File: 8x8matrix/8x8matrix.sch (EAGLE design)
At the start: 21 parts

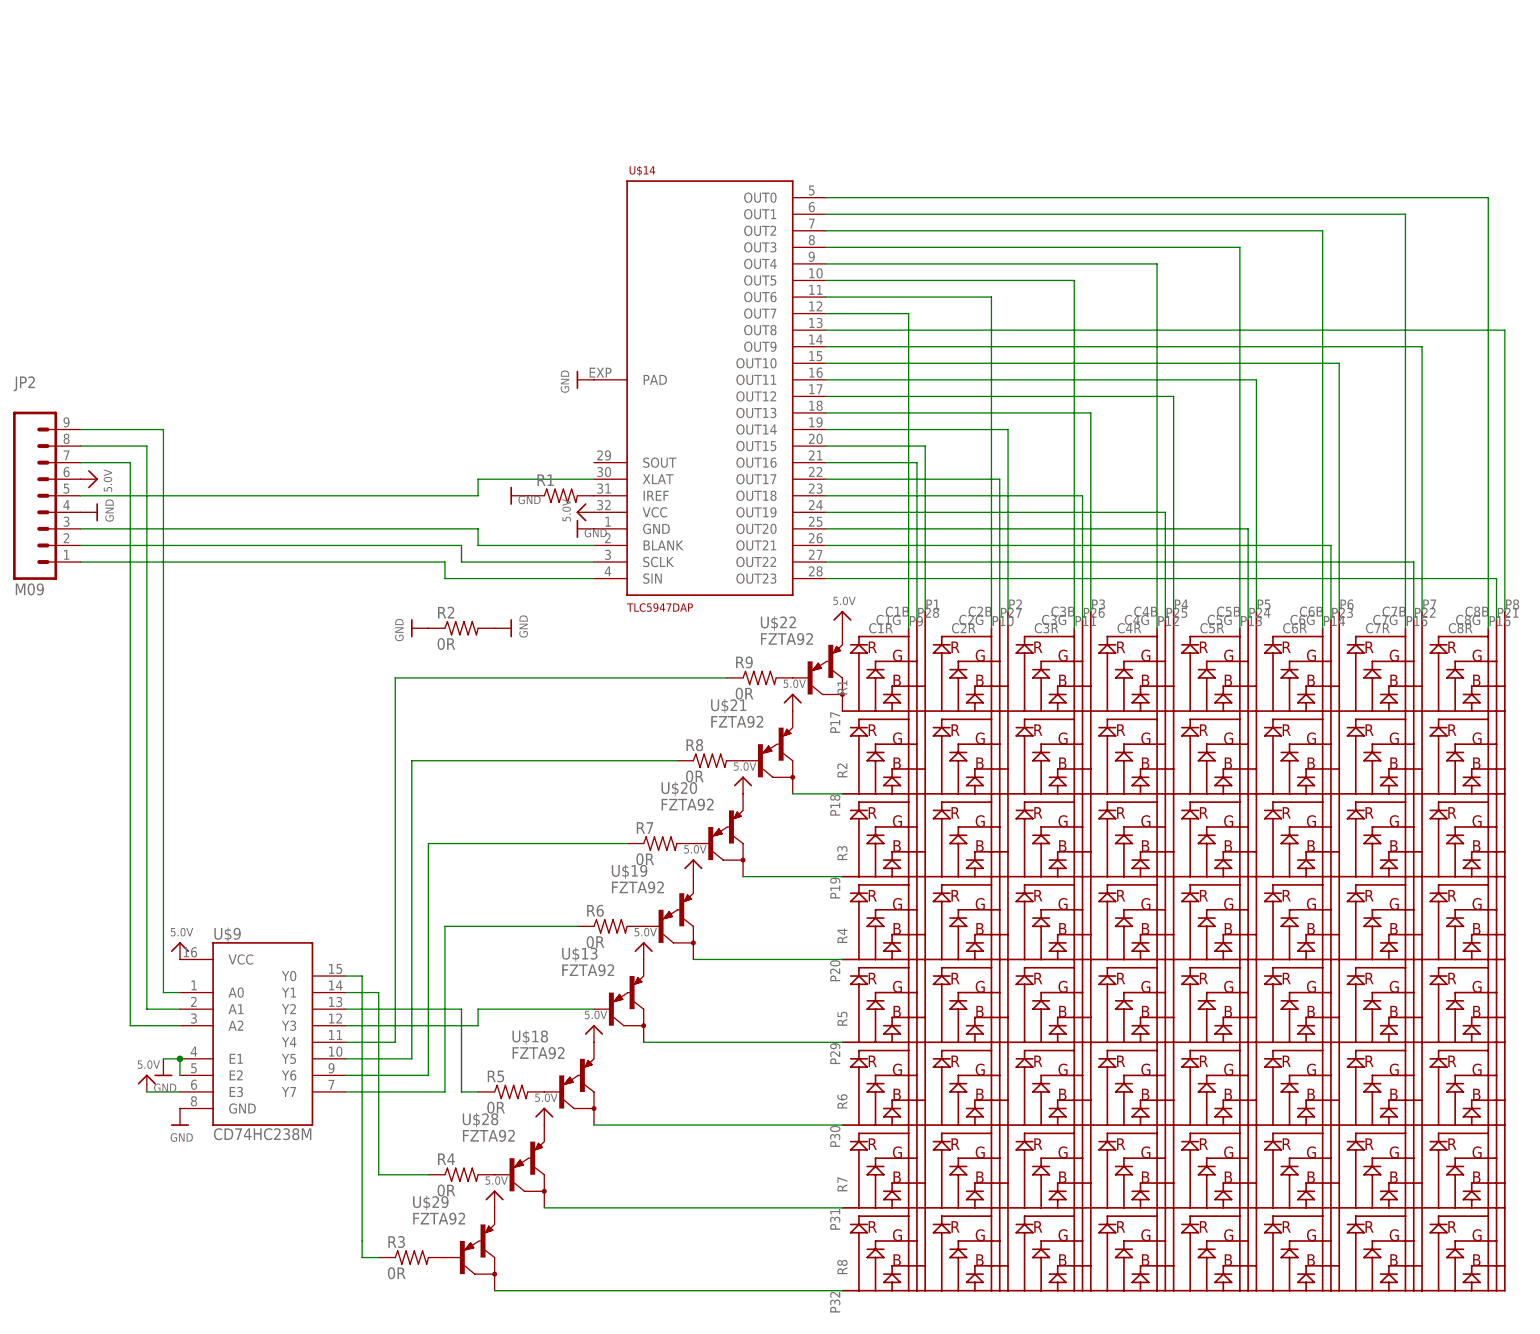
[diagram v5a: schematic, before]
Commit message: tried with regular SOT23 PNPs
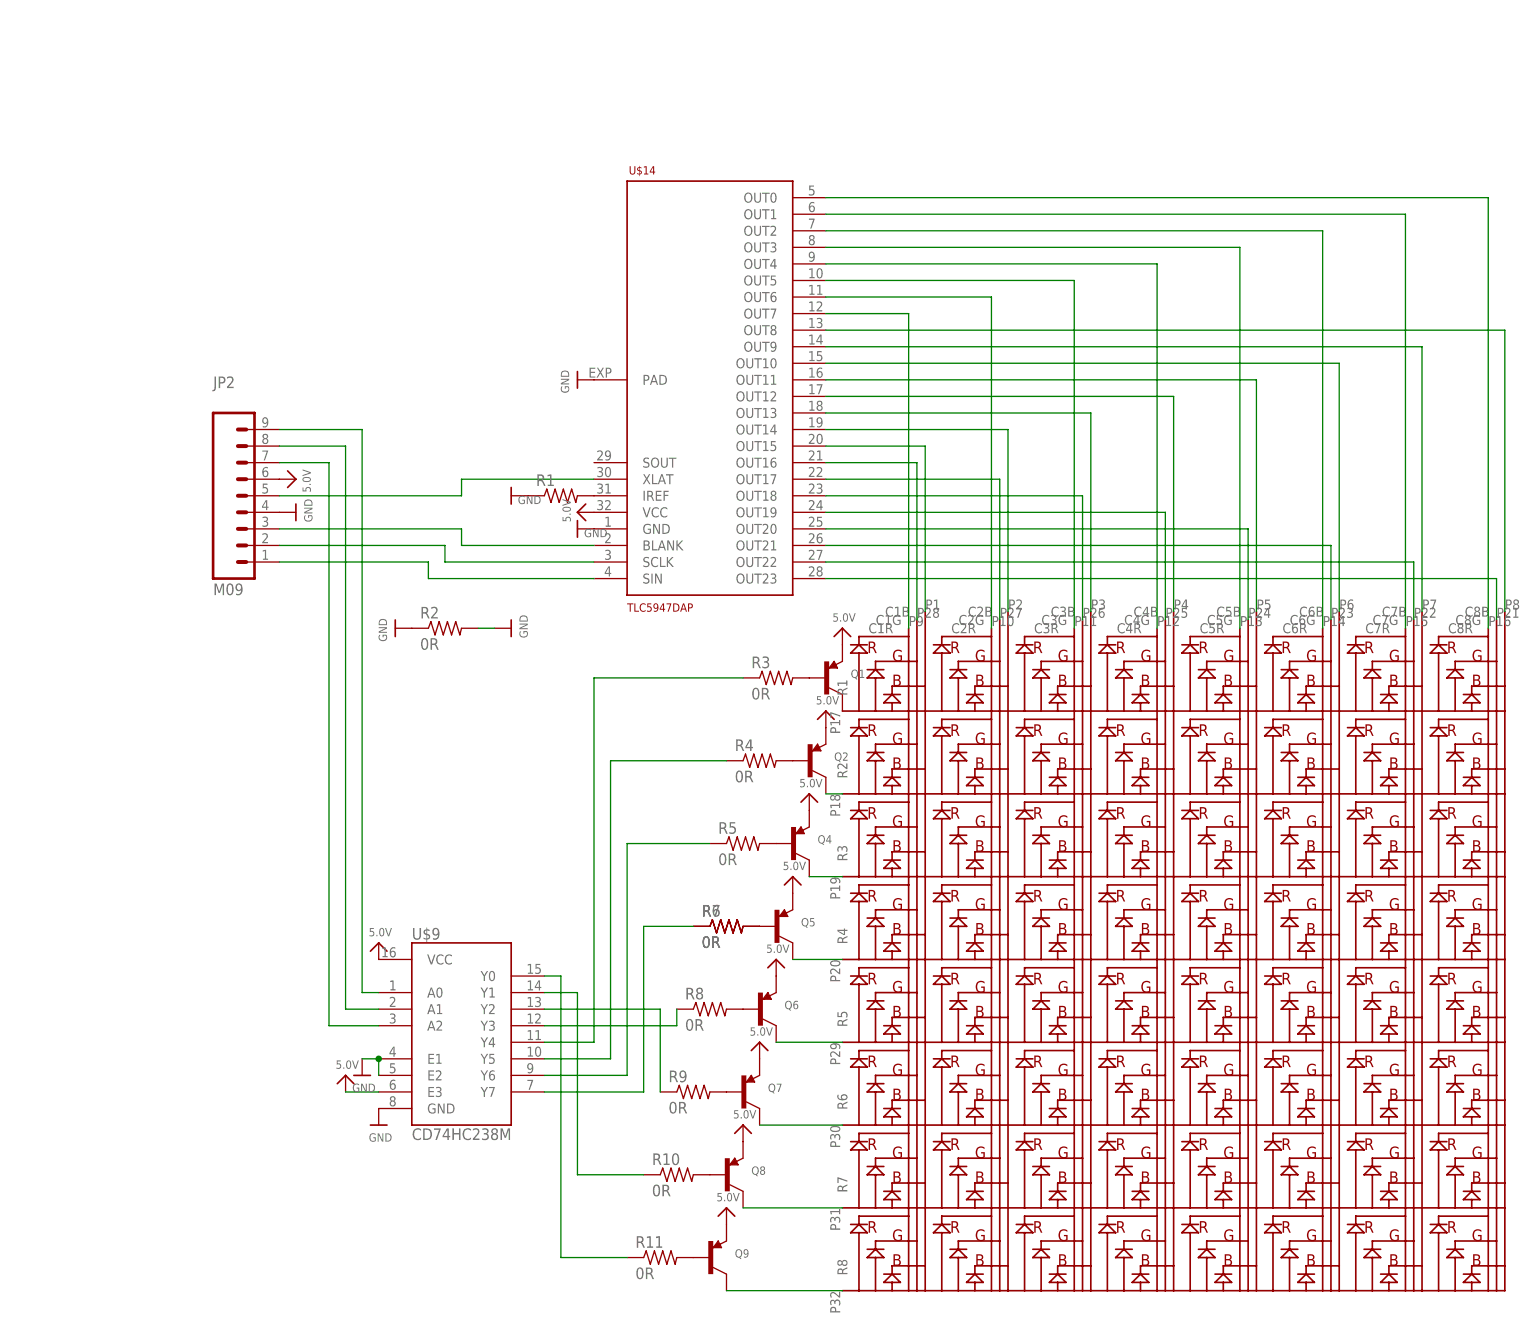
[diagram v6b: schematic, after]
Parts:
- removed U$13, U$18, U$19, U$20, U$21, U$22, U$28, U$29: FZTA92, mylib:FZTA92
- added Q1, Q2, Q4, Q5, Q6, Q7, Q8, Q9: (no value), microbuilder:TRANSISTOR_PNPSOT23-WAVE
- added R10, R11: 0R, resistor:R-US_M1206
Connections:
- new net N$52: Q9.C, U$1.R8
- net 5.0V: now also Q1.E, Q2.E, Q4.E, Q5.E, Q6.E, Q7.E, Q8.E, Q9.E; no longer U$13.E, U$18.E, U$19.E, U$20.E, U$21.E, U$22.E, U$28.E, U$29.E
- net N$25: no longer U$13.B
- net N$26: now also R7.1
- net N$28: now also Q1.C, U$1.R1; no longer R5.2, U$18.B
- net N$29: now also R5.1; no longer R7.1
- net N$30: now also R4.1; no longer R8.1
- net N$31: now also R3.1; no longer R9.1
- net N$32: now also Q4.B, R5.2; no longer U$1.R5, U$13.C
- net N$33: no longer R5.1
- net N$34: now also R10.1; no longer R4.1
- net N$35: now also R11.1; no longer R3.1
- net N$39: now also Q7.B, R9.2; no longer R7.2, U$20.B
- net N$40: now also Q8.B, R10.2; no longer R8.2, U$21.B
- net N$41: now also Q1.B, R3.2; no longer R9.2, U$22.B
- net N$42: now also Q2.B, R4.2; no longer U$1.R6, U$18.C
- net N$43: now also Q5.B, R6.2, R7.2; no longer U$1.R1, U$22.C
- net N$44: now also Q2.C; no longer U$21.C
- net N$45: now also Q6.B, R8.2; no longer R6.2, U$19.B
- net N$46: now also Q9.B, R11.2; no longer U$1.R3, U$20.C
- net N$47: now also Q5.C; no longer U$19.C
- net N$48: now also Q4.C, U$1.R3; no longer R4.2, U$28.B
- net N$49: now also Q6.C, U$1.R5; no longer R3.2, U$29.B
- net N$50: now also Q7.C, U$1.R6; no longer U$1.R7, U$28.C
- net N$51: now also Q8.C, U$1.R7; no longer U$1.R8, U$29.C
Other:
- moved on the sheet: JP2, R2, R3, R4, R5, R6, R7, R8, R9, U$9

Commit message: tried with BCR198S pnp arrays
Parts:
- removed Q1, Q2, Q4, Q5, Q6, Q7, Q8, Q9: (no value), microbuilder:TRANSISTOR_PNPSOT23-WAVE
- removed R10, R11, R3, R4, R5, R6, R7, R8, R9: 0R, resistor:R-US_M1206
- added U$13, U$17, U$18, U$19: BCR198S, mylib:BCR198S
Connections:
- removed net N$42: Q2.B, R4.2
- removed net N$43: Q5.B, R6.2, R7.2
- removed net N$44: Q2.C, U$1.R2
- removed net N$45: Q6.B, R8.2
- removed net N$46: Q9.B, R11.2
- removed net N$48: Q4.C, U$1.R3
- removed net N$49: Q6.C, U$1.R5
- removed net N$51: Q8.C, U$1.R7
- net 5.0V: now also R2.1, R2.2, U$13G$1.E, U$13G$2.E, U$17G$1.E, U$17G$2.E, U$18G$1.E, U$18G$2.E, U$19G$2.E; no longer Q1.E, Q2.E, Q4.E, Q5.E, Q6.E, Q7.E, Q8.E, Q9.E
- net GND: no longer R2.1, R2.2
- net N$25: now also U$18G$1.B
- net N$26: now also U$17G$2.B; no longer R6.1, R7.1
- net N$28: now also U$1.R3, U$17G$1.C; no longer Q1.C, U$1.R1
- net N$29: now also U$17G$1.B; no longer R5.1
- net N$30: now also U$13G$2.B; no longer R4.1
- net N$31: now also U$13G$1.B; no longer R3.1
- net N$32: now also U$1.R2, U$13G$2.C; no longer Q4.B, R5.2
- net N$33: now also U$18G$2.B
- net N$34: now also U$19G$1.B; no longer R10.1
- net N$35: now also U$19G$2.B; no longer R11.1
- net N$39: now also U$1.R1, U$13G$1.C; no longer Q7.B, R9.2
- net N$40: now also U$1.R5, U$18G$1.C; no longer Q8.B, R10.2
- net N$41: now also U$1.R7, U$19G$1.C; no longer Q1.B, R3.2
- net N$47: now also U$17G$2.C; no longer Q5.C
- net N$50: now also U$18G$2.C; no longer Q7.C
- net N$52: now also U$19G$2.C; no longer Q9.C

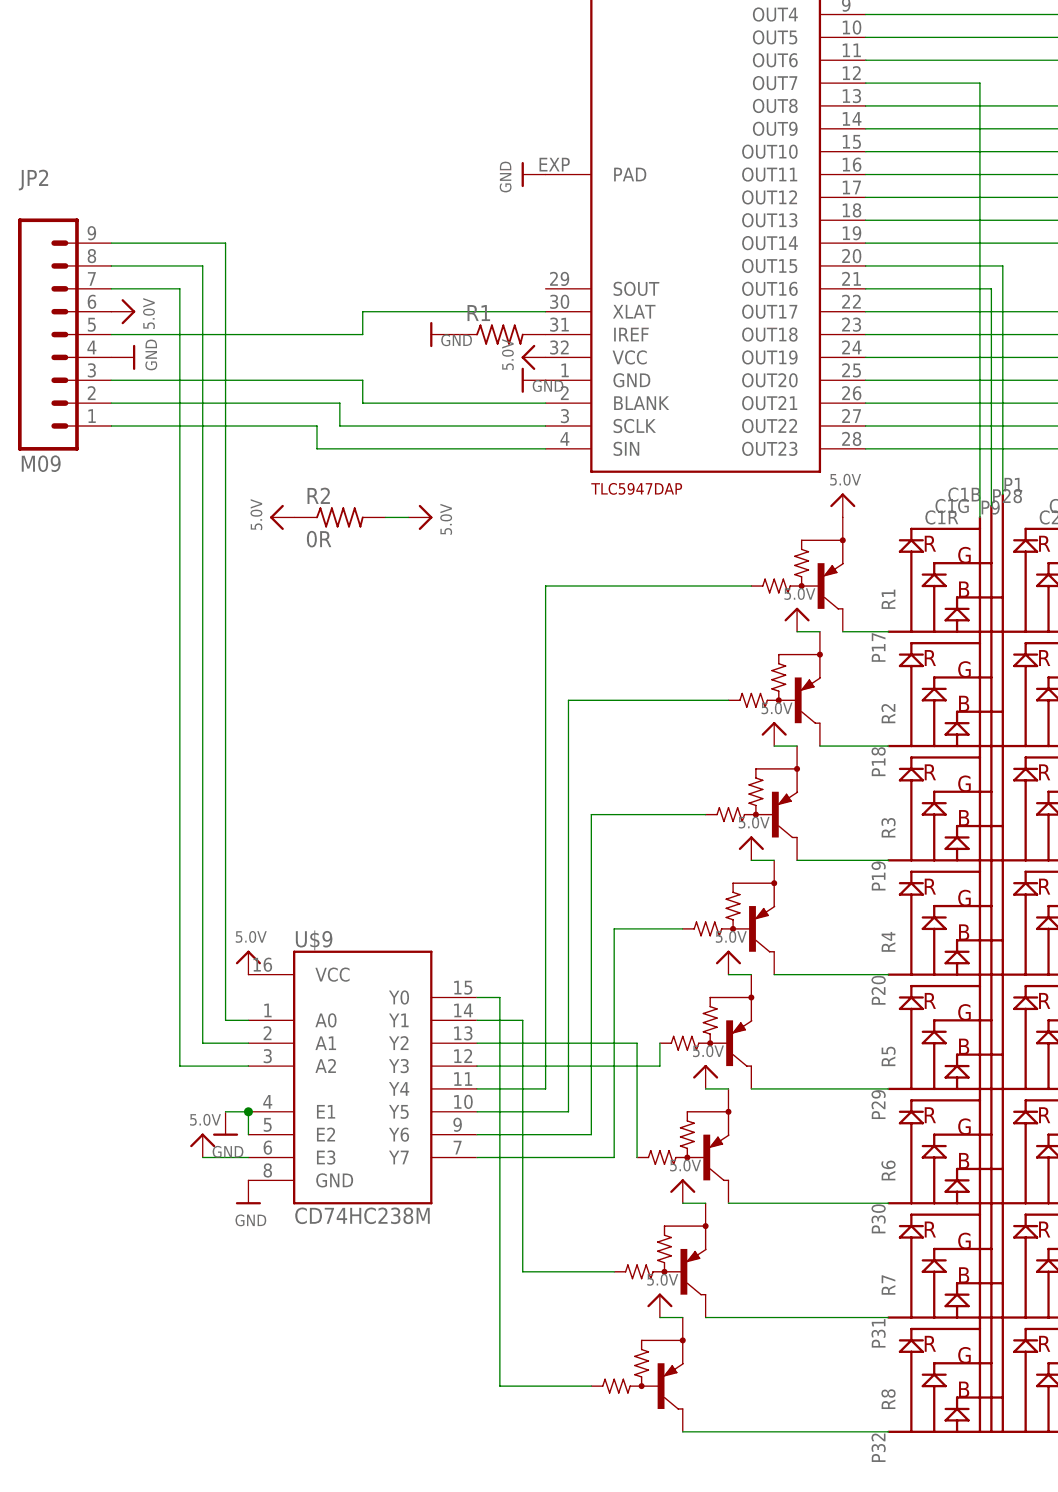
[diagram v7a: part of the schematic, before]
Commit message: found something that works: IRF7104
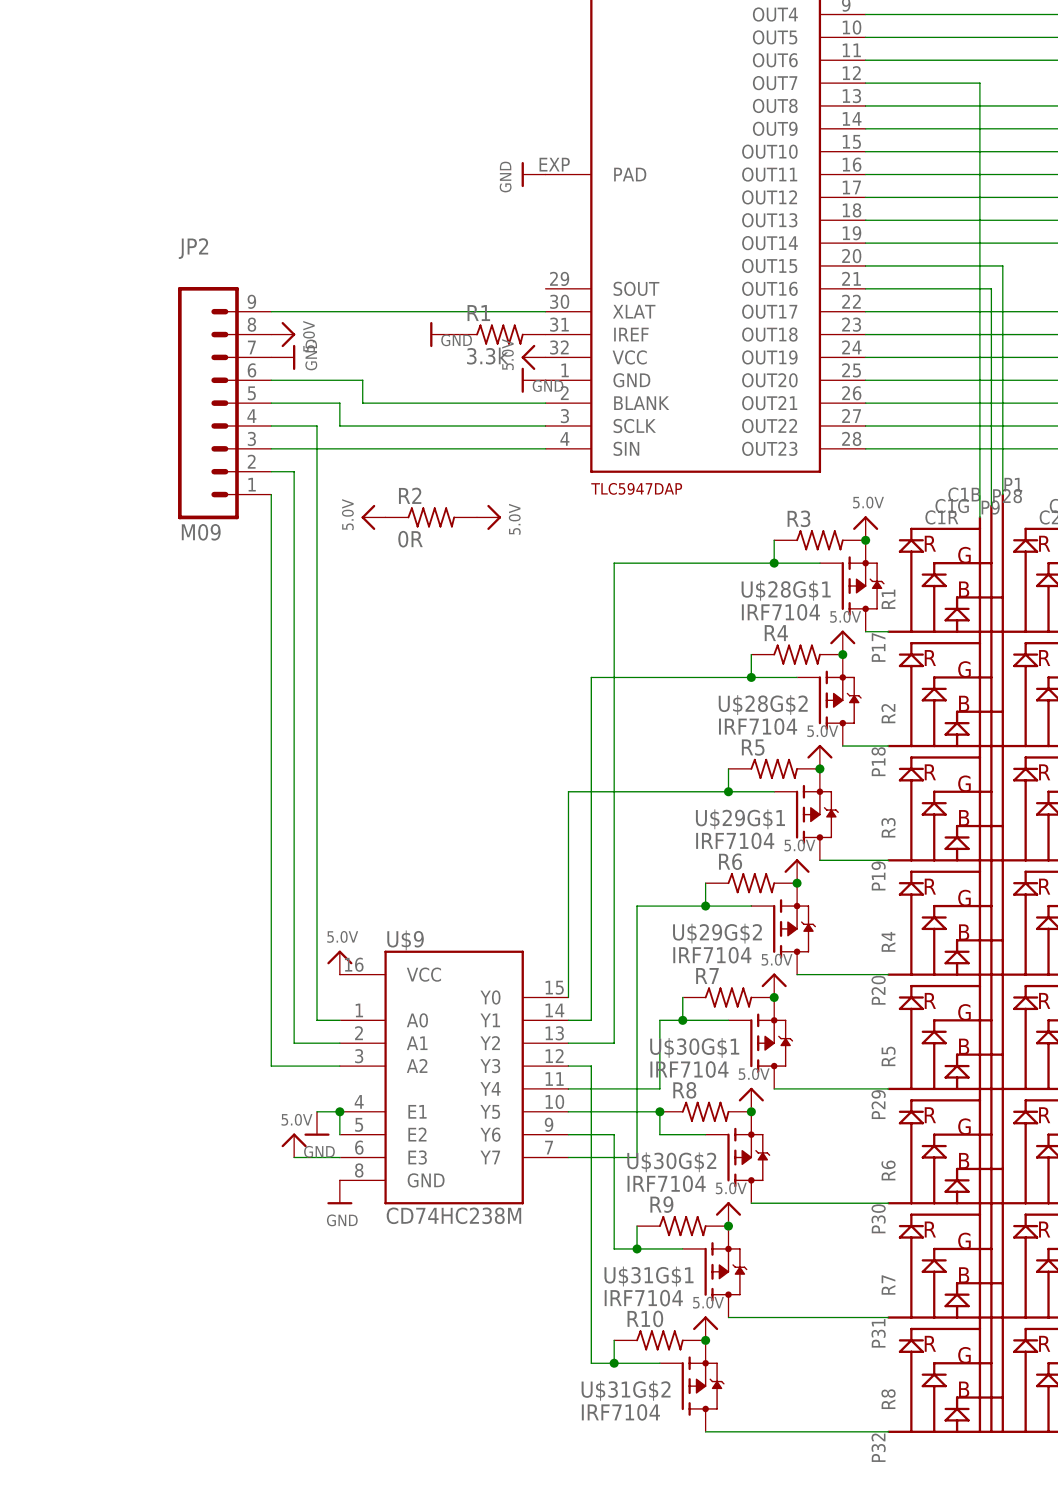
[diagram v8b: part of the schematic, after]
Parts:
- removed U$13, U$17, U$18, U$19: BCR198S, mylib:BCR198S
- added R10, R3, R4, R5, R6, R7, R8, R9: (no value), resistor:R-US_R0805
- added U$28, U$29, U$30, U$31: IRF7104, mylib:IRF7104
- R1: value (none) -> 3.3k
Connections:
- removed net N$25: U$18G$1.B, U$9.Y3
- removed net N$26: U$17G$2.B, U$9.Y7
- removed net N$29: U$17G$1.B, U$9.Y6
- removed net N$30: U$13G$2.B, U$9.Y5
- removed net N$31: U$13G$1.B, U$9.Y4
- removed net N$33: U$18G$2.B, U$9.Y2
- removed net N$34: U$19G$1.B, U$9.Y1
- removed net N$35: U$19G$2.B, U$9.Y0
- removed net N$47: U$1.R4, U$17G$2.C
- new net N$42: U$1.R4, U$29G$2.D
- new net Y0: R5.1, U$29G$1.G, U$9.Y0
- new net Y1: R4.1, U$28G$2.G, U$9.Y1
- new net Y2: R3.1, U$28G$1.G, U$9.Y2
- new net Y3: R10.1, U$31G$2.G, U$9.Y3
- new net Y4: R7.1, U$30G$1.G, U$9.Y4
- new net Y5: R8.1, U$30G$2.G, U$9.Y5
- new net Y6: R9.1, U$31G$1.G, U$9.Y6
- new net Y7: R6.1, U$29G$2.G, U$9.Y7
- net 5.0V: now also JP2.8, R10.2, R3.2, R4.2, R5.2, R6.2, R7.2, R8.2, R9.2, U$28G$1.S, U$28G$2.S, U$29G$1.S, U$29G$2.S, U$30G$1.S, U$30G$2.S, U$31G$1.S, U$31G$2.S; no longer JP2.6, U$13G$1.E, U$13G$2.E, U$17G$1.E, U$17G$2.E, U$18G$1.E, U$18G$2.E, U$19G$2.E
- net BLANK: now also JP2.6; no longer JP2.3
- net GND: now also JP2.7; no longer JP2.4
- net N$28: now also U$29G$1.D; no longer U$17G$1.C
- net N$32: now also U$28G$2.D; no longer U$13G$2.C
- net N$36: now also JP2.3; no longer JP2.9
- net N$37: now also JP2.2; no longer JP2.8
- net N$38: now also JP2.1; no longer JP2.7
- net N$39: now also U$28G$1.D; no longer U$13G$1.C
- net N$40: now also U$30G$1.D; no longer U$18G$1.C
- net N$41: now also U$31G$1.D; no longer U$19G$1.C
- net N$50: now also U$30G$2.D; no longer U$18G$2.C
- net N$52: now also U$31G$2.D; no longer U$19G$2.C
- net SCLK: now also JP2.5; no longer JP2.2
- net SIN: now also JP2.4; no longer JP2.1
- net XLAT: now also JP2.9; no longer JP2.5
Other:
- moved on the sheet: JP2, R2, U$9
